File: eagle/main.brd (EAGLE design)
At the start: 100 x 95 mm, 33 parts, among them IC1 STM32F103, IC2 LM1117, Q1 8MHz

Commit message: Fix errors in main module schematic
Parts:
- added C11: 1uF, rcl:C025-025X050
- added C12: 0.1uF, rcl:C025-025X050
- C7, C8: value (none) -> 30pF
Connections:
- removed net VBAT: IC1.1
- net 3.3V: now also C11.1, C12.1, IC1.1
- net GND: now also C11.2, C12.2, U1.SHLD1, U1.SHLD2, U1.SHLD3
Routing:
- net 3.3V: track 172.6 -> 195.6 mm
- net GND: track 78.7 -> 89.0 mm
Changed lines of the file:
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@@
 <drawing>
 <settings>
-<setting alwaysvectorfont="yes"/>
+<setting alwaysvectorfont="no"/>
 <setting verticaltext="up"/>
 </settings>
@@
 <attribute name="VALUE" x="45.706" y="56.286" size="1.27" layer="27" ratio="10" rot="R270"/>
 </element>
-<element name="C7" library="rcl" library_urn="urn:adsk.eagle:library:334" package="C025-025X050" package3d_urn="urn:adsk.eagle:package:23629/2" value="" x="33" y="33" smashed="yes" rot="R90">
+<element name="C7" library="rcl" library_urn="urn:adsk.eagle:library:334" package="C025-025X050" package3d_urn="urn:adsk.eagle:package:23629/2" value="30pF" x="33" y="33" smashed="yes" rot="R90">
 <attribute name="NAME" x="31.476" y="30.714" size="1.27" layer="25" ratio="10" rot="R90"/>
 <attribute name="SPICEPREFIX" value="C" x="138.41" y="118.09" size="1.778" layer="27" rot="R90" display="off"/>
 <attribute name="VALUE" x="35.794" y="30.714" size="1.27" layer="27" ratio="10" rot="R90"/>
 </element>
-<element name="C8" library="rcl" library_urn="urn:adsk.eagle:library:334" package="C025-025X050" package3d_urn="urn:adsk.eagle:package:23629/2" value="" x="37" y="33" smashed="yes" rot="R90">
+<element name="C8" library="rcl" library_urn="urn:adsk.eagle:library:334" package="C025-025X050" package3d_urn="urn:adsk.eagle:package:23629/2" value="30pF" x="37" y="33" smashed="yes" rot="R90">
 <attribute name="NAME" x="35.476" y="30.714" size="1.27" layer="25" ratio="10" rot="R90"/>
 <attribute name="SPICEPREFIX" value="C" x="142.41" y="124.44" size="1.778" layer="27" rot="R90" display="off"/>
@@
 <attribute name="VALUE" x="9.19" y="81.325" size="1.27" layer="27"/>
 </element>
+<element name="C11" library="rcl" library_urn="urn:adsk.eagle:library:334" package="C025-025X050" package3d_urn="urn:adsk.eagle:package:23629/2" value="1uF" x="25" y="51.5" smashed="yes">
+<attribute name="NAME" x="22.714" y="53.024" size="1.27" layer="25" ratio="10"/>
+<attribute name="SPICEPREFIX" value="C" x="25" y="51.5" size="1.778" layer="27" display="off"/>
+<attribute name="VALUE" x="22.714" y="48.706" size="1.27" layer="27" ratio="10"/>
+</element>
+<element name="C12" library="rcl" library_urn="urn:adsk.eagle:library:334" package="C025-025X050" package3d_urn="urn:adsk.eagle:package:23629/2" value="0.1uF" x="25.5" y="38.5" smashed="yes" rot="R180">
+<attribute name="NAME" x="27.786" y="36.976" size="1.27" layer="25" ratio="10" rot="R180"/>
+<attribute name="SPICEPREFIX" value="C" x="25.5" y="38.5" size="1.778" layer="27" rot="R180" display="off"/>
+<attribute name="VALUE" x="27.786" y="41.294" size="1.27" layer="27" ratio="10" rot="R180"/>
+</element>
 </elements>
 <signals>
-<signal name="VBAT">
-<contactref element="IC1" pad="1"/>
-</signal>
 <signal name="GND">
 <contactref element="C2" pad="2"/>
@@
 <contactref element="C8" pad="1"/>
 <contactref element="C9" pad="2"/>
-<contactref element="IC1" pad="12"/>
 <contactref element="RESET" pad="4"/>
 <contactref element="RESET" pad="3"/>
@@
 <wire x1="37.27" y1="59.5" x2="36.5" y2="59.5" width="0.1524" layer="1"/>
 <wire x1="36.5" y1="59.5" x2="35.75" y2="58.75" width="0.1524" layer="1"/>
-<wire x1="40.75" y1="44.25" x2="40.75" y2="42.48" width="0.1524" layer="1"/>
 <wire x1="40.75" y1="42.48" x2="42.73" y2="40.5" width="0.1524" layer="1"/>
 <wire x1="29.38" y1="48.06" x2="29.94" y2="48.06" width="0.1524" layer="1"/>
@@
 <wire x1="43.75" y1="53.25" x2="44.75" y2="53.25" width="0.1524" layer="1"/>
 <wire x1="42.46335625" y1="51.96335625" x2="43.75" y2="53.25" width="0.1524" layer="1"/>
-<wire x1="38.8232875" y1="46.75" x2="40.75" y2="44.8232875" width="0.1524" layer="1"/>
+<wire x1="42.46335625" y1="46.53664375" x2="42.6767125" y2="46.75" width="0.1524" layer="1"/>
+<contactref element="U1" pad="SHLD3"/>
+<contactref element="U1" pad="SHLD1"/>
+<contactref element="U1" pad="SHLD2"/>
+<wire x1="78.85" y1="93.2" x2="80.5" y2="93.2" width="0.1524" layer="1"/>
+<wire x1="80.5" y1="93.2" x2="82.53" y2="93.2" width="0.1524" layer="1"/>
+<wire x1="86.21" y1="93.2" x2="82.53" y2="93.2" width="0.1524" layer="1"/>
+<wire x1="81.23" y1="90.5" x2="81.23" y2="92.47" width="0.1524" layer="1"/>
+<wire x1="81.23" y1="92.47" x2="80.5" y2="93.2" width="0.1524" layer="1"/>
+<contactref element="C11" pad="2"/>
+<contactref element="IC1" pad="12"/>
+<wire x1="40.75" y1="44.25" x2="40.75" y2="42.48" width="0.1524" layer="1"/>
+<contactref element="C12" pad="2"/>
+<wire x1="40.75" y1="44.8232875" x2="38.8232875" y2="46.75" width="0.1524" layer="1"/>
 <wire x1="40.75" y1="44.25" x2="40.75" y2="44.8232875" width="0.1524" layer="1"/>
 <wire x1="40.75" y1="44.8232875" x2="42.46335625" y2="46.53664375" width="0.1524" layer="1"/>
-<wire x1="42.46335625" y1="46.53664375" x2="42.6767125" y2="46.75" width="0.1524" layer="1"/>
 </signal>
 <signal name="VCC">
@@
 </signal>
 <signal name="N$5">
-<contactref element="IC1" pad="5"/>
 <contactref element="Q1" pad="2"/>
 <contactref element="C7" pad="2"/>
-<wire x1="37.25" y1="44.25" x2="37.25" y2="42.25" width="0.1524" layer="1"/>
 <wire x1="37.25" y1="42.25" x2="34" y2="39" width="0.1524" layer="1"/>
 <wire x1="34" y1="39" x2="32.46" y2="39" width="0.1524" layer="1"/>
 <wire x1="33" y1="34.27" x2="33" y2="38" width="0.1524" layer="1"/>
 <wire x1="33" y1="38" x2="34" y2="39" width="0.1524" layer="1"/>
+<contactref element="IC1" pad="5"/>
+<wire x1="37.25" y1="44.25" x2="37.25" y2="42.25" width="0.1524" layer="1"/>
 </signal>
 <signal name="N$7">
-<contactref element="IC1" pad="6"/>
 <contactref element="Q1" pad="1"/>
 <contactref element="C8" pad="2"/>
+<wire x1="37" y1="34.27" x2="37" y2="38.46" width="0.1524" layer="1"/>
+<wire x1="37" y1="38.46" x2="37.27" y2="38.73" width="0.1524" layer="1"/>
+<contactref element="IC1" pad="6"/>
+<wire x1="37.27" y1="38.73" x2="37.54" y2="39" width="0.1524" layer="1"/>
 <wire x1="37.75" y1="44.25" x2="37.75" y2="39.21" width="0.1524" layer="1"/>
 <wire x1="37.75" y1="39.21" x2="37.54" y2="39" width="0.1524" layer="1"/>
-<wire x1="37" y1="34.27" x2="37" y2="38.46" width="0.1524" layer="1"/>
-<wire x1="37" y1="38.46" x2="37.54" y2="39" width="0.1524" layer="1"/>
 </signal>
 <signal name="3.3V">
@@
 <wire x1="28" y1="46.9" x2="28" y2="52.77" width="0.4" layer="1"/>
 <wire x1="28" y1="52.77" x2="34.73" y2="59.5" width="0.4" layer="1"/>
+<wire x1="47" y1="62" x2="42.19" y2="66.81" width="0.4" layer="1"/>
+<wire x1="42.19" y1="66.81" x2="42.19" y2="78.81" width="0.4" layer="1"/>
+<wire x1="42.19" y1="78.81" x2="42.19" y2="91.5" width="0.4" layer="1"/>
+<wire x1="31.5" y1="89.5" x2="31.54" y2="89.54" width="0.4" layer="1"/>
+<wire x1="31.5" y1="89.5" x2="42.19" y2="78.81" width="0.4" layer="1"/>
+<wire x1="23.73" y1="51.17" x2="28" y2="46.9" width="0.4" layer="1"/>
 <contactref element="R2" pad="2"/>
 <contactref element="C9" pad="1"/>
 <contactref element="IC1" pad="13"/>
 <contactref element="JP1" pad="3"/>
-<wire x1="47" y1="62" x2="42.19" y2="66.81" width="0.4" layer="1"/>
-<wire x1="42.19" y1="66.81" x2="42.19" y2="78.81" width="0.4" layer="1"/>
-<wire x1="42.19" y1="78.81" x2="42.19" y2="91.5" width="0.4" layer="1"/>
-<wire x1="31.54" y1="91.5" x2="31.54" y2="89.54" width="0.4" layer="1"/>
-<wire x1="31.54" y1="89.54" x2="31.5" y2="89.5" width="0.4" layer="1"/>
-<wire x1="31.5" y1="89.5" x2="42.19" y2="78.81" width="0.4" layer="1"/>
+<contactref element="C11" pad="1"/>
 <wire x1="41.25" y1="44.25" x2="41.25" y2="42.75" width="0.1524" layer="1"/>
-<wire x1="30.52" y1="45.52" x2="29.38" y2="45.52" width="0.1524" layer="1"/>
-<wire x1="29.38" y1="45.52" x2="28" y2="46.9" width="0.4" layer="1"/>
-<wire x1="65.026" y1="45.68" x2="70.4" y2="45.68" width="0.1524" layer="1"/>
-<wire x1="70.4" y1="45.68" x2="70.44" y2="45.72" width="0.1524" layer="1"/>
+<wire x1="28" y1="46.9" x2="29.38" y2="45.52" width="0.4" layer="1"/>
+<wire x1="30.52" y1="45.52" x2="29.5" y2="45.52" width="0.1524" layer="1"/>
+<wire x1="29.5" y1="45.52" x2="29.38" y2="45.52" width="0.1524" layer="1"/>
+<wire x1="31.54" y1="89.54" x2="31.54" y2="91.5" width="0.4" layer="1"/>
+<wire x1="70.44" y1="45.72" x2="65.066" y2="45.72" width="0.1524" layer="1"/>
+<wire x1="65.066" y1="45.72" x2="65.026" y2="45.68" width="0.1524" layer="1"/>
+<wire x1="23.73" y1="51.5" x2="23.73" y2="51.17" width="0.4" layer="1"/>
+<contactref element="IC1" pad="1"/>
+<contactref element="C12" pad="1"/>
+<wire x1="35.25" y1="44.25" x2="35.25" y2="43.25" width="0.1524" layer="1"/>
+<wire x1="34" y1="42" x2="33.5" y2="42" width="0.1524" layer="1"/>
+<wire x1="33.02" y1="42" x2="30" y2="42" width="0.1524" layer="1"/>
+<wire x1="30" y1="42" x2="26.77" y2="38.77" width="0.1524" layer="1"/>
+<wire x1="26.77" y1="38.77" x2="26.77" y2="38.5" width="0.1524" layer="1"/>
+<wire x1="35.25" y1="43.25" x2="34" y2="42" width="0.1524" layer="1"/>
+<wire x1="33.5" y1="42" x2="33.02" y2="42" width="0.1524" layer="1"/>
+<wire x1="33.02" y1="42" x2="29.5" y2="45.52" width="0.1524" layer="1"/>
 </signal>
 <signal name="N$6">

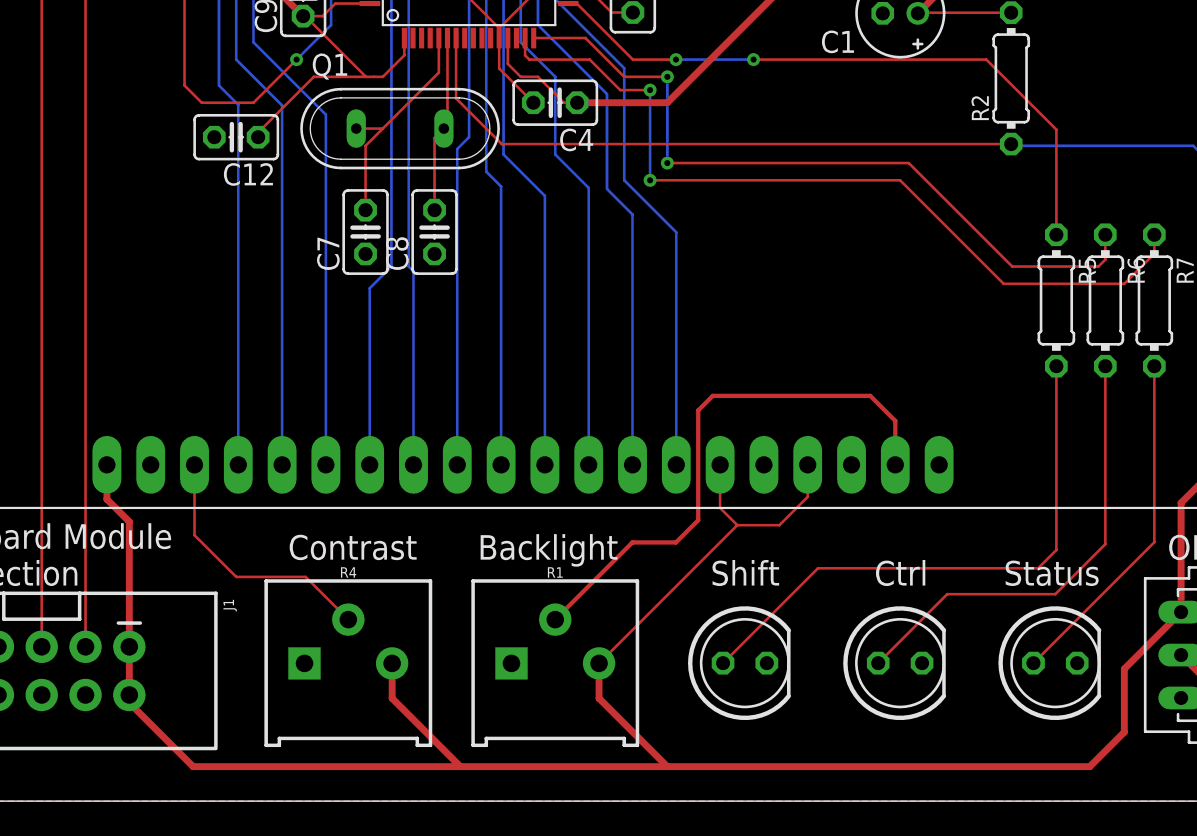
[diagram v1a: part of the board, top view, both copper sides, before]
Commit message: Partially fix error with LCD library in main board
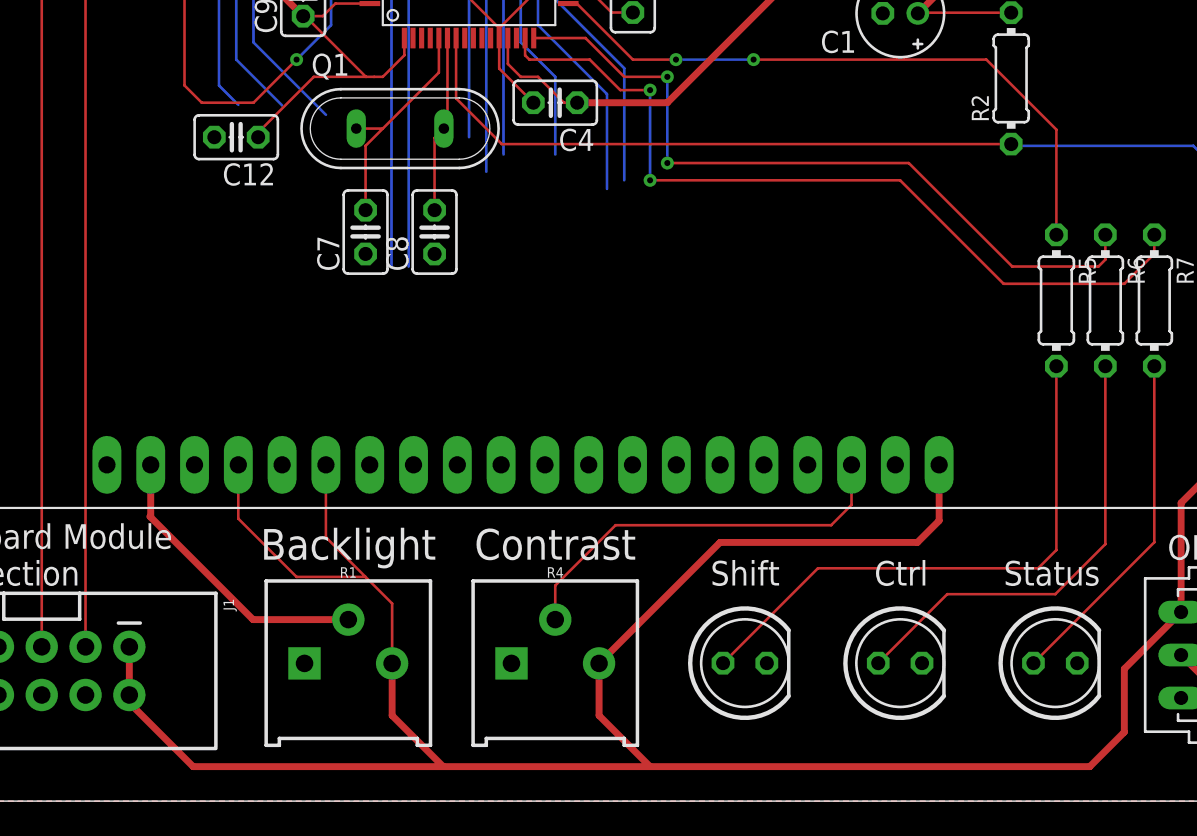
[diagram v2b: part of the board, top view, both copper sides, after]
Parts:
- moved R1 12.0 mm to (32.0, 8.00)
- moved R4 12.0 mm to (44.0, 8.00)
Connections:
- net DB0: now also GLCD2.7; no longer GLCD2.P$7
- net DB1: now also GLCD2.8; no longer GLCD2.P$8
- net DB2: now also GLCD2.9; no longer GLCD2.P$9
- net DB3: now also GLCD2.10; no longer GLCD2.P$10
- net DB4: now also GLCD2.11; no longer GLCD2.P$11
- net DB5: now also GLCD2.12; no longer GLCD2.P$12
- net DB6: now also GLCD2.13; no longer GLCD2.P$13
- net DB7: now also GLCD2.14; no longer GLCD2.P$14
- net EN: now also GLCD2.6; no longer GLCD2.P$6
- net GND: now also GLCD2.2, GLCD2.20; no longer GLCD2.P$2, GLCD2.P$20
- net N$1: now also GLCD2.19; no longer GLCD2.P$19
- net N$2: now also GLCD2.3; no longer GLCD2.P$3
- net RS: now also GLCD2.4; no longer GLCD2.P$4
- net RW: now also GLCD2.5; no longer GLCD2.P$5
- net VCC: now also GLCD2.1, GLCD2.15, GLCD2.17; no longer GLCD2.P$1, GLCD2.P$15, GLCD2.P$17
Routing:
- net RS: track 39.7 -> 18.8 mm
- net RW: track 38.8 -> 18.0 mm
- net EN: track 38.0 -> 17.7 mm
- net DB2: track 41.5 -> 22.3 mm
- net DB4: track 43.5 -> 24.5 mm
- net DB5: track 44.3 -> 25.5 mm
- net DB7: track 43.6 -> 25.8 mm
- net VCC: track 223.0 -> 240.6 mm
- net DB3: track 42.6 -> 25.3 mm
- net DB6: track 44.5 -> 27.8 mm
- net N$1: track 32.0 -> 17.0 mm
- net DB0: track 41.3 -> 29.2 mm
- net DB1: track 41.3 -> 29.7 mm
- net N$2: track 15.0 -> 23.4 mm

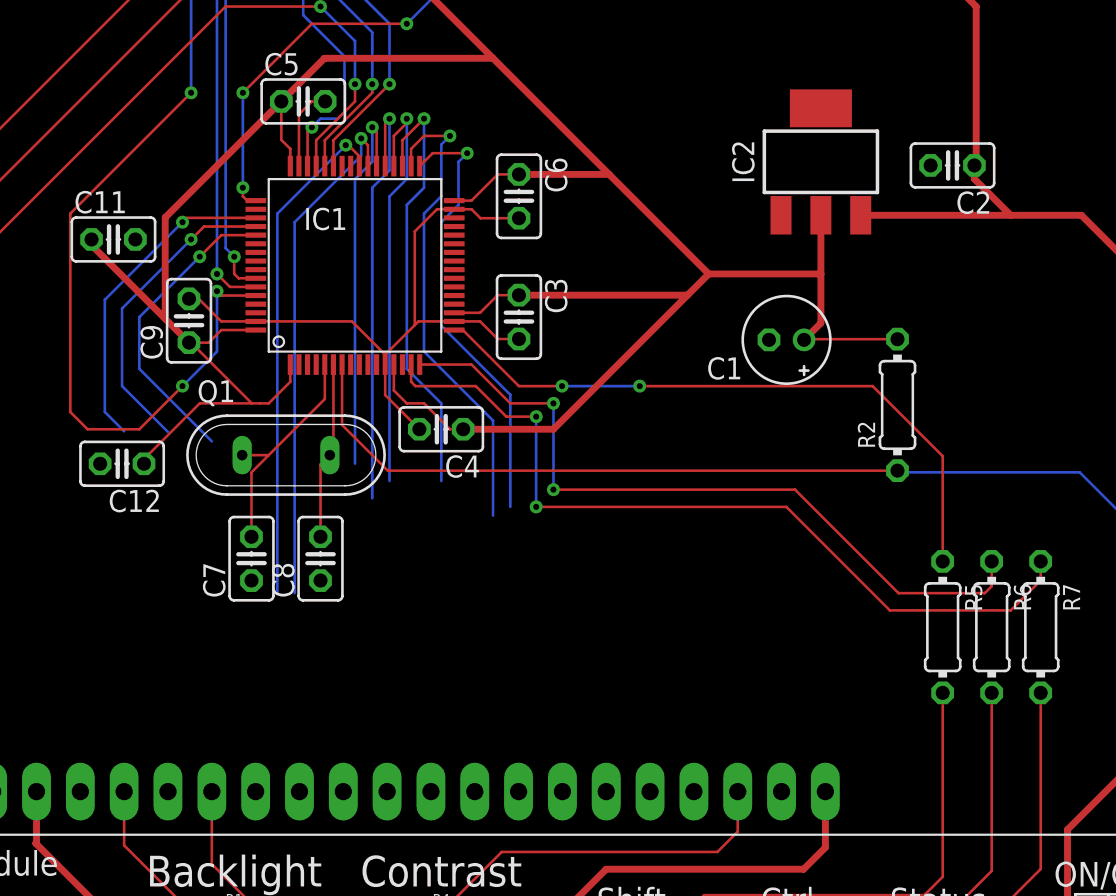
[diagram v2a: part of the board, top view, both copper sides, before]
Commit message: Re-route LCD to fix errors
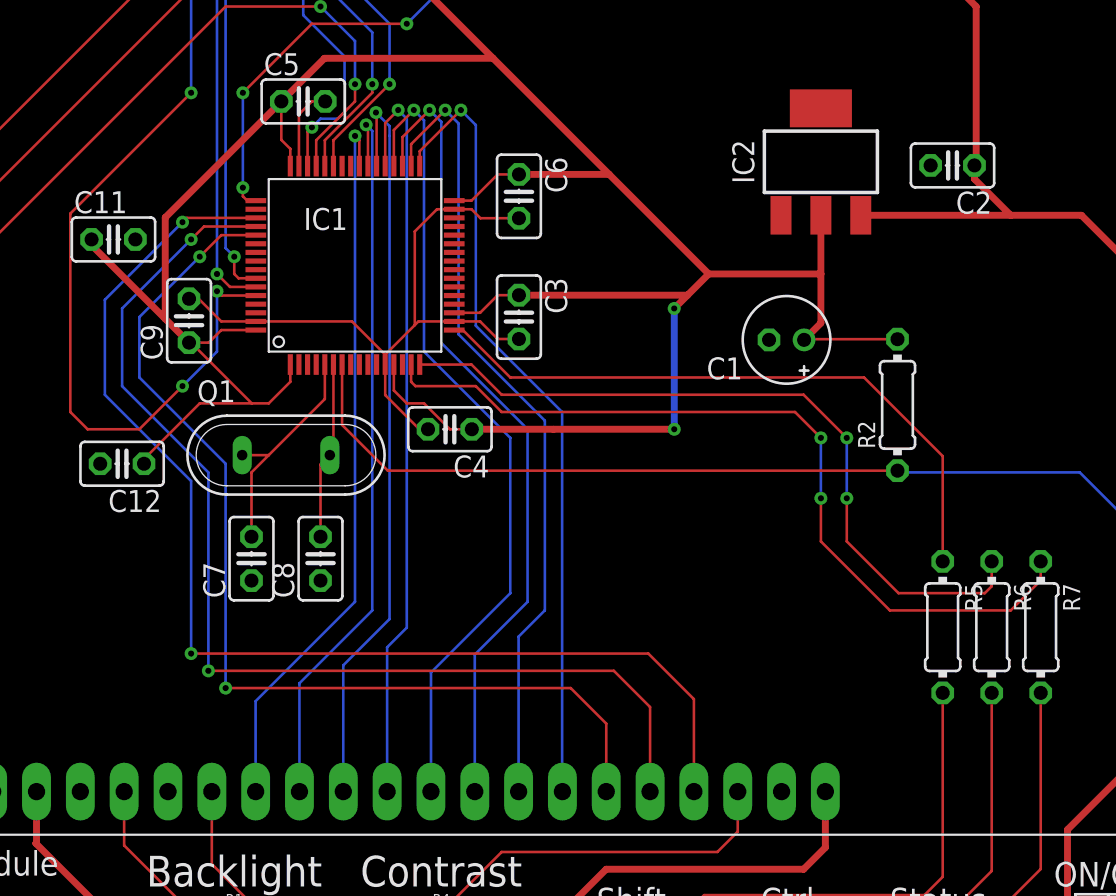
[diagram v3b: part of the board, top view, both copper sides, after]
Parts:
- moved C4 0.50 mm to (44.5, 40.5)
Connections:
- net DB0: now also IC1.33; no longer IC1.40
- net DB1: now also IC1.34; no longer IC1.39
- net DB2: now also IC1.35; no longer IC1.38
- net DB3: now also IC1.36; no longer IC1.37
- net DB4: now also IC1.37; no longer IC1.36
- net DB5: now also IC1.38; no longer IC1.35
- net DB6: now also IC1.39; no longer IC1.34
- net DB7: now also IC1.40; no longer IC1.33
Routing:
- net RS: track 18.8 -> 68.9 mm, vias 1 -> 2
- net RW: track 18.0 -> 64.2 mm, vias 1 -> 2
- net EN: track 17.7 -> 59.1 mm, vias 1 -> 2
- net DB2: track 22.3 -> 47.0 mm
- net DB3: track 25.3 -> 47.5 mm
- net DB4: track 24.5 -> 43.7 mm
- net DB5: track 25.5 -> 43.9 mm
- net DB0: track 29.2 -> 46.2 mm
- net DB1: track 29.7 -> 46.6 mm
- net DB7: track 25.8 -> 42.2 mm
- net DB6: track 27.8 -> 43.0 mm
- net 3.3V: track 195.6 -> 199.7 mm, vias 0 -> 2
- net N$13: track 43.2 -> 43.8 mm
- net GND: track 89.0 -> 89.5 mm
- net N$14: vias 2 -> 0
